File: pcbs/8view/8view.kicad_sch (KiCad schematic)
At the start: 47 parts, among them J1 Conn_01x10_Female, J2 Conn_01x10_Female, J3 Conn_01x06_Female, J4 Conn_01x06_Female, U1 ATtiny828-A, U2 HDSP-A151, U3 HDSP-A151

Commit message: 8view: caps++
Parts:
- added C1, C2: 1p, Capacitor_SMD:C_0603_1608Metric, symbol Device:C
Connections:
- net +5V: now also C1.1, C2.1
- net GND: now also C1.2, C2.2

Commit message: 8view: v1.1 touches
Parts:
- D1, D2, D3, D4: value LED -> GREEN
- D5, D6, D7, D8: value LED -> RED
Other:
- moved on the sheet: D1, D2, D3, D4, D5, D6, D7, D8, R1, R2, R3, R4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

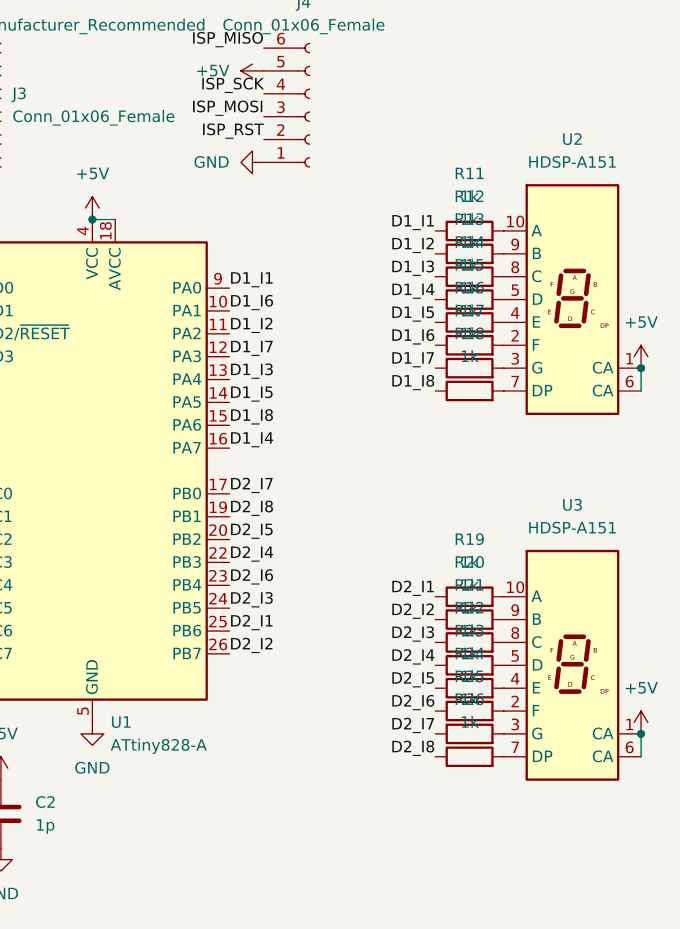
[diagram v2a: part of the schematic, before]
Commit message: 8view: flipped mode
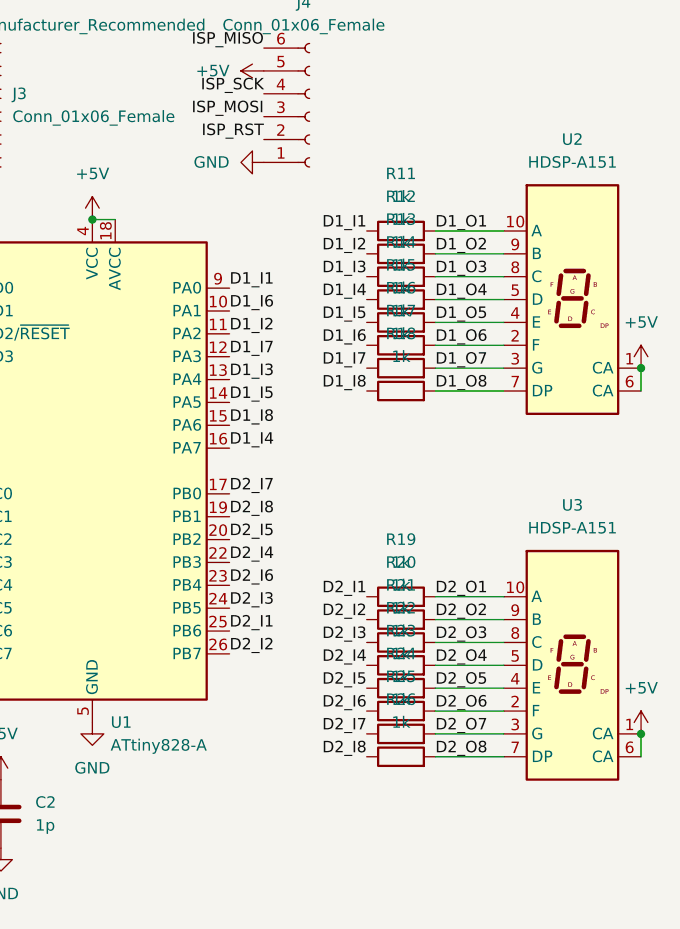
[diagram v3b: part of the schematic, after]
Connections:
- net D1_O7: now reaches R17.2, U2.3 (G)
- net D2_O8: now reaches R26.2, U3.7 (DP)
- net D1_O2: now reaches R12.2, U2.9 (B)
- net D1_O6: now reaches R16.2, U2.2 (F)
- net D1_O1: now reaches R11.2, U2.10 (A)
- net D1_O5: now reaches R15.2, U2.4 (E)
- net D1_O4: now reaches R14.2, U2.5 (D)
- net D1_O8: now reaches R18.2, U2.7 (DP)
- net D1_O3: now reaches R13.2, U2.8 (C)
- net D2_O6: now reaches R24.2, U3.2 (F)
- net D2_O2: now reaches R20.2, U3.9 (B)
- net D2_O1: now reaches R19.2, U3.10 (A)
- net D2_O7: now reaches R25.2, U3.3 (G)
- net D2_O5: now reaches R23.2, U3.4 (E)
- net D2_O4: now reaches R22.2, U3.5 (D)
- net D2_O3: now reaches R21.2, U3.8 (C)
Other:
- moved on the sheet: R11, R12, R13, R14, R15, R16, R17, R18, R19, R20, R21, R22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
